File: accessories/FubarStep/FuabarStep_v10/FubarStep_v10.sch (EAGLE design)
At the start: 10 parts, among them IC1 7805, X1 DC21MMX

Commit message: More work.
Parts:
- removed AD: (no value), pinhead:PINHD-1X6
- removed IOL, POWER: (no value), pinhead:PINHD-1X8
- added C10, C11, C12, C13, C14, C15, C18, C19, C8, C9: .1uF, SparkFun-Capacitors:CAPPTH
- added C16, C17, C5: 100uF, SparkFun-Capacitors:CAP_POLPTH1
- added IC2, IC3: SN754410NE, texas:L293E
- added JP10, JP11, JP12, JP13, JP14, JP15, JP16, JP17, JP18, JP19, JP20, JP21, JP22, JP23, JP24, JP25, JP26, JP27, JP3, JP4, JP5, JP6: (no value), SparkFun-Connectors:M03LOCK
- added JP2: (no value), SparkFun-Connectors:M04SCREW_LOCK
- added JP7, JP8, JP9: (no value), SparkFun-Connectors:M04LOCK
- added LOGO1: OSHW-LOGOM, SparkFun-Aesthetics:OSHW-LOGOM
- C2: value 10uF -> 100uF; device SparkFun-Capacitors:CAP_POLPTH2 -> SparkFun-Capacitors:CAP_POLPTH1
- IC1: value 7805 -> OKI-78SR-5/1.5-W36H-C
- JP1: device pinhead:PINHD-1X10 -> SparkFun-Connectors:M04SCREW_LOCK
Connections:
- removed net AD0: AD.1
- removed net AD1: AD.2
- removed net AD2: AD.3
- removed net AD3: AD.4
- removed net AD4: AD.5
- removed net AD4/SDA: JP1.9
- removed net AD5: AD.6
- removed net AD5/SCL: JP1.10
- removed net AREF: JP1.8
- removed net IO0: IOL.1
- removed net IO1: IOL.2
- removed net IO2: IOL.3
- removed net IO3: IOL.4
- removed net IO4: IOL.5
- removed net IO5: IOL.6
- removed net IO6: IOL.7
- removed net IO7: IOL.8
- removed net IO8: JP1.1
- removed net IO9: JP1.2
- removed net MISO: JP1.5
- removed net MOSI: JP1.4
- removed net SCK: JP1.6
- removed net SS: JP1.3
- new net M1A1: IC2.1A
- new net M1A2: IC2.2A
- new net M1A3: IC2.3A
- new net M1A4: IC2.4A
- new net M1EN12: IC2.1-2EN, U$1.PIN7
- new net M1EN34: IC2.3-4EN, U$1.PIN8
- new net M1O1: C10.2, IC2.1Y, JP1.1
- new net M1O2: C11.2, IC2.2Y, JP1.2
- new net M1O3: C12.1, IC2.3Y, JP1.3
- new net M1O4: C9.1, IC2.4Y, JP1.4
- new net M2A1: IC3.1A
- new net M2A2: IC3.2A
- new net M2A3: IC3.3A
- new net M2A4: IC3.4A
- new net M2EN12: IC3.1-2EN, U$1.PIN9
- new net M2EN34: IC3.3-4EN, U$1.PIN10
- new net M2O1: C8.2, IC3.1Y, JP2.1
- new net M2O2: C13.2, IC3.2Y, JP2.2
- new net M2O3: C15.1, IC3.3Y, JP2.3
- new net M2O4: C14.1, IC3.4Y, JP2.4
- new net N$12: JP8.1
- new net N$2: JP18.1
- new net N$29: JP9.1
- new net N$3: JP19.1
- new net N$67: JP9.2
- new net N$68: JP9.3
- new net N$69: JP23.1
- new net N$87: JP22.1
- new net N$88: JP17.1
- new net N$89: JP16.1
- new net N$90: JP15.1
- new net N$91: JP14.1
- new net N$92: JP10.1
- new net N$93: JP11.1
- new net N$94: JP12.1
- new net N$95: JP13.1
- new net N$96: JP24.1
- new net N$97: JP25.1
- new net RX: JP7.3, U$1.PIN28
- new net SERVO1: JP6.1
- new net SERVO2: JP3.1
- new net SERVO3: JP4.1
- new net SERVO4: JP5.1
- new net TX: JP7.2, U$1.PIN29
- net +3V3: no longer POWER.4
- net +5V: now also C18.1, C19.1, C5.+, IC2.VCC1, IC3.VCC1, JP10.2, JP11.2, JP12.2, JP13.2, JP14.2, JP15.2, JP16.2, JP17.2, JP18.2, JP19.2, JP20.2, JP21.2, JP22.2, JP23.2, JP24.2, JP25.2, JP26.2, JP27.2, JP3.2, JP4.2, JP5.2, JP6.2, JP7.1, U$1.VIN, U$2.VIN; no longer POWER.2, POWER.5, U$1.5V_OUT, U$2.5V_OUT
- net GND: now also C10.1, C11.1, C12.2, C13.1, C14.2, C15.2, C16.-, C17.-, C18.2, C19.2, C5.-, C8.1, C9.2, IC2.GND1, IC2.GND2, IC2.GND3, IC2.GND4, IC3.GND1, IC3.GND2, IC3.GND3, IC3.GND4, JP10.3, JP11.3, JP12.3, JP13.3, JP14.3, JP15.3, JP16.3, JP17.3, JP18.3, JP19.3, JP20.3, JP21.3, JP22.3, JP23.3, JP24.3, JP25.3, JP26.3, JP27.3, JP3.3, JP4.3, JP5.3, JP6.3, JP7.4, JP8.4, JP9.4; no longer JP1.7, POWER.6, POWER.7
- net N$11: now also JP20.1; no longer U$1.PIN7
- net N$13: now also JP8.2; no longer U$1.PIN8
- net N$14: now also JP8.3; no longer U$1.PIN9
- net N$15: now also JP21.1; no longer U$1.PIN10
- net N$33: now also JP26.1; no longer U$1.PIN29
- net N$34: now also JP27.1; no longer U$1.PIN28
- net RESET: no longer POWER.3
- net VIN: now also C16.+, C17.+, IC2.VCC2, IC3.VCC2; no longer POWER.8, U$1.VIN, U$2.VIN
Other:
- note added: "Fubarino Stepper Shield"
- note removed: "0"
- note removed: "1"
- note removed: "10"
- note removed: "11"
- note removed: "12"
- note removed: "13"
- note removed: "2"
- note removed: "3"
- note removed: "4"
- note removed: "5"
- note removed: "6"
- note removed: "7"
- note removed: "8"
- note removed: "9"
- note removed: "Fubarino Arduino Uno Adapter Board"
- note removed: "SCL"
- note removed: "SDA"
- moved on the sheet: C1, C2, IC1, U$1, U$2

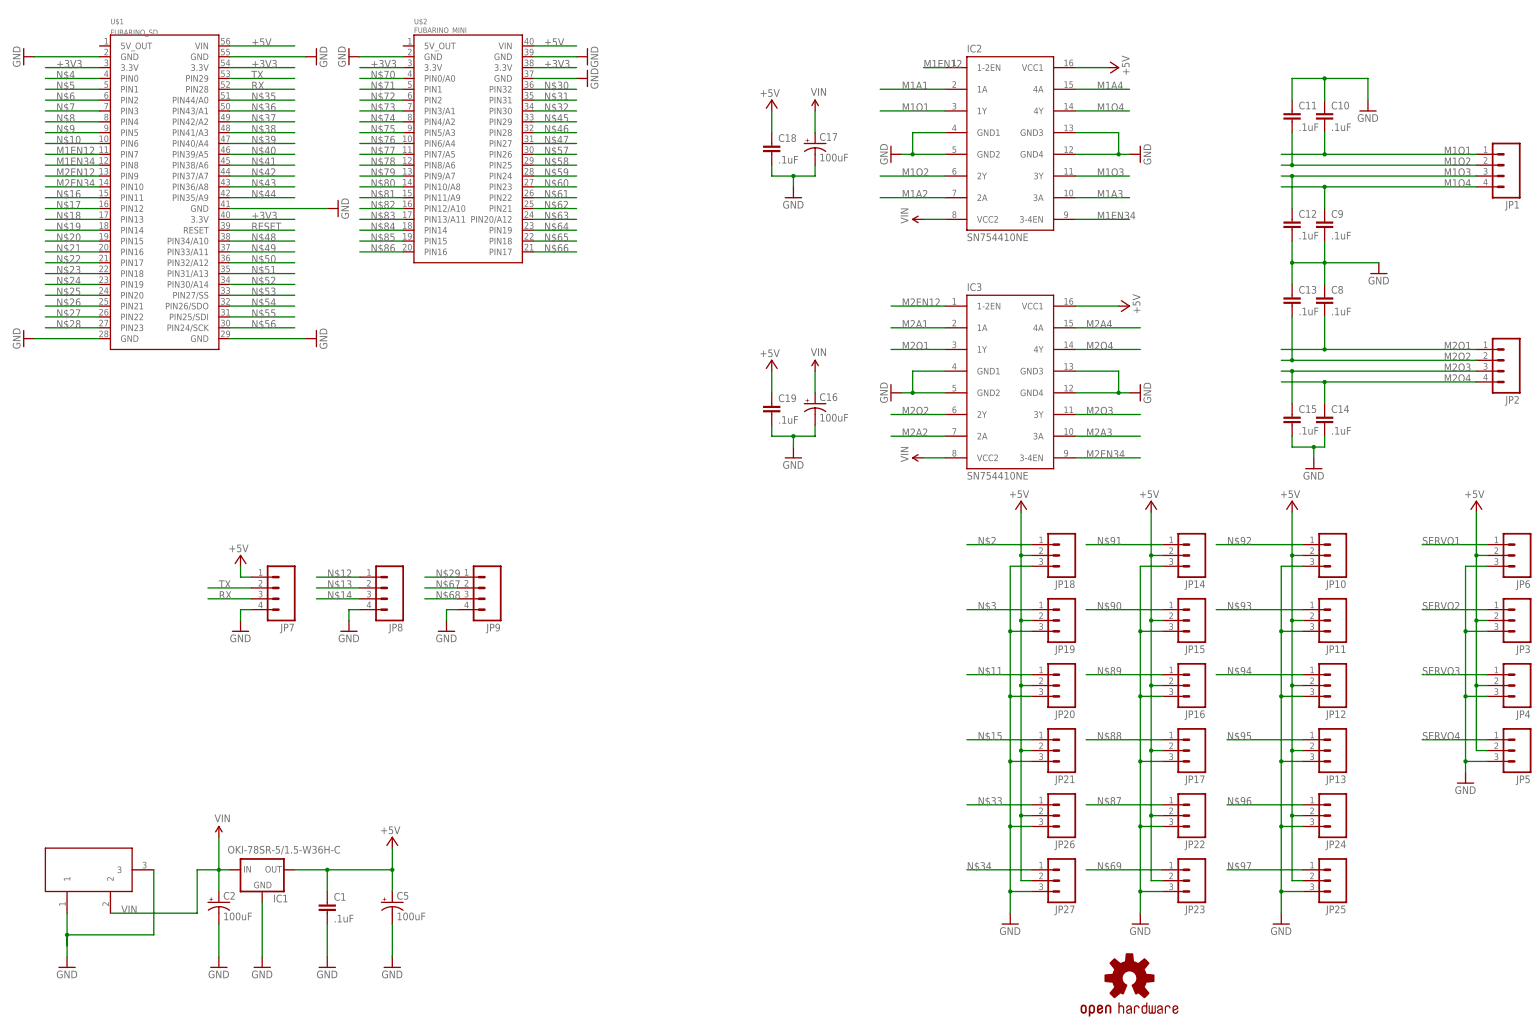
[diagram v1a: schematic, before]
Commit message: Renamed board from thin to normal, added all Mini routing except for 2 pins (maybe TX/RX?) Almost done!
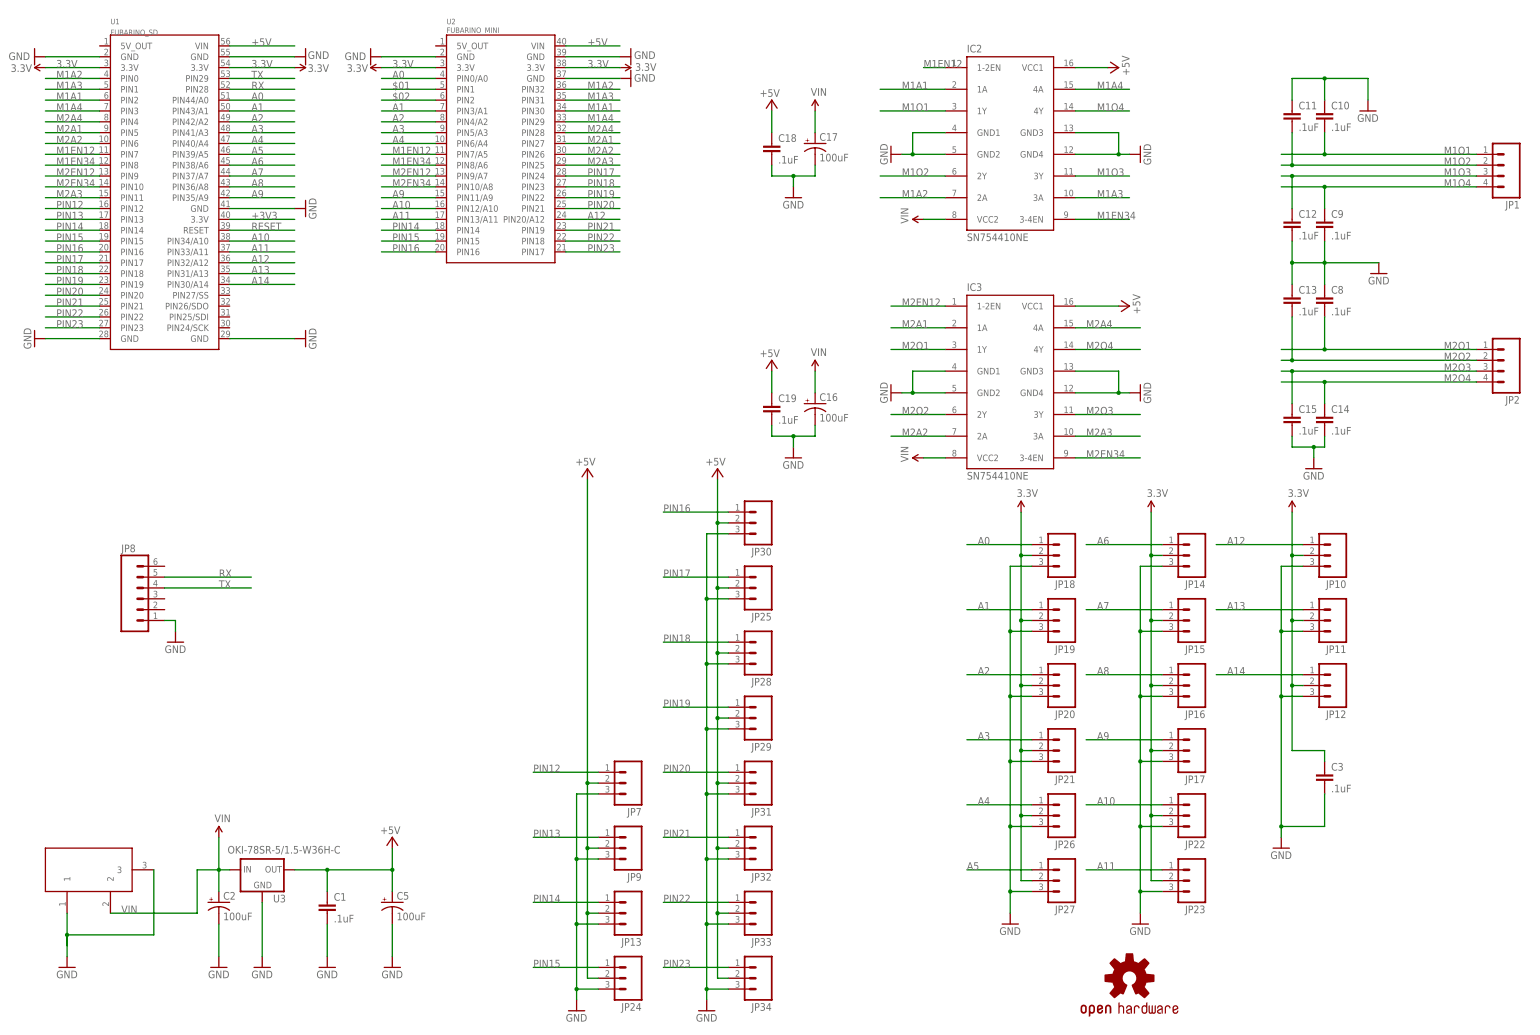
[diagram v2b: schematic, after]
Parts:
- removed IC1: OKI-78SR-5/1.5-W36H-C, SparkFun-PowerIC:V_REG_78XXSIDE
- removed JP3, JP4, JP5, JP6: (no value), SparkFun-Connectors:M03LOCK
- removed U$2: FUBARINO_MINI, SchmalzHausPublic:FUBARINO_MINI
- added C3: .1uF, SparkFun-Capacitors:CAPPTH
- added JP28, JP29, JP30, JP31, JP32, JP33, JP34: (no value), SparkFun-Connectors:M03PTH
- added U2: FUBARINO_MINI, SchmalzHausPublic:FUBARINO_MINI
- added U3: OKI-78SR-5/1.5-W36H-C, SparkFun-PowerIC:V_REG_78XXSINK
- JP10, JP11, JP12, JP13, JP14, JP15, JP16, JP17, JP18, JP19, JP20, JP21, JP22, JP23, JP24, JP25, JP26, JP27: device SparkFun-Connectors:M03LOCK -> SparkFun-Connectors:M03PTH
- JP7, JP9: device SparkFun-Connectors:M04LOCK -> SparkFun-Connectors:M03PTH
- JP8: device SparkFun-Connectors:M04LOCK -> SparkFun-Connectors:M06LOCK
- renumbered U$1 to U1
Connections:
- removed net N$10: U1.PIN6
- removed net N$11: JP20.1
- removed net N$12: JP8.1
- removed net N$13: JP8.2
- removed net N$14: JP8.3
- removed net N$15: JP21.1
- removed net N$16: U1.PIN11
- removed net N$17: U1.PIN12
- removed net N$18: U1.PIN13
- removed net N$19: U1.PIN14
- removed net N$2: JP18.1
- removed net N$20: U1.PIN15
- removed net N$21: U1.PIN16
- removed net N$22: U1.PIN17
- removed net N$23: U1.PIN18
- removed net N$24: U1.PIN19
- removed net N$25: U1.PIN20
- removed net N$26: U1.PIN21
- removed net N$27: U1.PIN22
- removed net N$28: U1.PIN23
- removed net N$29: JP9.1
- removed net N$3: JP19.1
- removed net N$30: U$2.PIN32
- removed net N$31: U$2.PIN31
- removed net N$32: U$2.PIN30
- removed net N$33: JP26.1
- removed net N$34: JP27.1
- removed net N$35: U1.PIN44/A0
- removed net N$36: U1.PIN43/A1
- removed net N$37: U1.PIN42/A2
- removed net N$38: U1.PIN41/A3
- removed net N$39: U1.PIN40/A4
- removed net N$4: U1.PIN0
- removed net N$40: U1.PIN39/A5
- removed net N$41: U1.PIN38/A6
- removed net N$42: U1.PIN37/A7
- removed net N$43: U1.PIN36/A8
- removed net N$44: U1.PIN35/A9
- removed net N$45: U$2.PIN29
- removed net N$46: U$2.PIN28
- removed net N$47: U$2.PIN27
- removed net N$48: U1.PIN34/A10
- removed net N$49: U1.PIN33/A11
- removed net N$5: U1.PIN1
- removed net N$50: U1.PIN32/A12
- removed net N$51: U1.PIN31/A13
- removed net N$52: U1.PIN30/A14
- removed net N$53: U1.PIN27/SS
- removed net N$54: U1.PIN26/SDO
- removed net N$55: U1.PIN25/SDI
- removed net N$56: U1.PIN24/SCK
- removed net N$57: U$2.PIN26
- removed net N$58: U$2.PIN25
- removed net N$59: U$2.PIN24
- removed net N$6: U1.PIN2
- removed net N$60: U$2.PIN23
- removed net N$61: U$2.PIN22
- removed net N$62: U$2.PIN21
- removed net N$63: U$2.PIN20/A12
- removed net N$64: U$2.PIN19
- removed net N$65: U$2.PIN18
- removed net N$66: U$2.PIN17
- removed net N$67: JP9.2
- removed net N$68: JP9.3
- removed net N$69: JP23.1
- removed net N$7: U1.PIN3
- removed net N$70: U$2.PIN0/A0
- removed net N$71: U$2.PIN1
- removed net N$72: U$2.PIN2
- removed net N$73: U$2.PIN3/A1
- removed net N$74: U$2.PIN4/A2
- removed net N$75: U$2.PIN5/A3
- removed net N$76: U$2.PIN6/A4
- removed net N$77: U$2.PIN7/A5
- removed net N$78: U$2.PIN8/A6
- removed net N$79: U$2.PIN9/A7
- removed net N$8: U1.PIN4
- removed net N$80: U$2.PIN10/A8
- removed net N$81: U$2.PIN11/A9
- removed net N$82: U$2.PIN12/A10
- removed net N$83: U$2.PIN13/A11
- removed net N$84: U$2.PIN14
- removed net N$85: U$2.PIN15
- removed net N$86: U$2.PIN16
- removed net N$87: JP22.1
- removed net N$88: JP17.1
- removed net N$89: JP16.1
- removed net N$9: U1.PIN5
- removed net N$90: JP15.1
- removed net N$91: JP14.1
- removed net N$92: JP10.1
- removed net N$93: JP11.1
- removed net N$94: JP12.1
- removed net N$95: JP13.1
- removed net N$96: JP24.1
- removed net N$97: JP25.1
- removed net SERVO1: JP6.1
- removed net SERVO2: JP3.1
- removed net SERVO3: JP4.1
- removed net SERVO4: JP5.1
- new net $01: U2.PIN1
- new net $02: U2.PIN2
- new net 3.3V: C3.1, JP10.2, JP11.2, JP12.2, JP14.2, JP15.2, JP16.2, JP17.2, JP18.2, JP19.2, JP20.2, JP21.2, JP22.2, JP23.2, JP26.2, JP27.2, U1.3.3V@1, U1.3.3V@3, U2.3.3V@1, U2.3.3V@3
- new net A0: JP18.1, U1.PIN44/A0, U2.PIN0/A0
- new net A1: JP19.1, U1.PIN43/A1, U2.PIN3/A1
- new net A10: JP22.1, U1.PIN34/A10, U2.PIN12/A10
- new net A11: JP23.1, U1.PIN33/A11, U2.PIN13/A11
- new net A12: JP10.1, U1.PIN32/A12, U2.PIN20/A12
- new net A13: JP11.1, U1.PIN31/A13
- new net A14: JP12.1, U1.PIN30/A14
- new net A2: JP20.1, U1.PIN42/A2, U2.PIN4/A2
- new net A3: JP21.1, U1.PIN41/A3, U2.PIN5/A3
- new net A4: JP26.1, U1.PIN40/A4, U2.PIN6/A4
- new net A5: JP27.1, U1.PIN39/A5
- new net A6: JP14.1, U1.PIN38/A6
- new net A7: JP15.1, U1.PIN37/A7
- new net A8: JP16.1, U1.PIN36/A8
- new net A9: JP17.1, U1.PIN35/A9, U2.PIN11/A9
- new net PIN12: JP7.1, U1.PIN12
- new net PIN13: JP9.1, U1.PIN13
- new net PIN14: JP13.1, U1.PIN14, U2.PIN14
- new net PIN15: JP24.1, U1.PIN15, U2.PIN15
- new net PIN16: JP30.1, U1.PIN16, U2.PIN16
- new net PIN17: JP25.1, U1.PIN17, U2.PIN24
- new net PIN18: JP28.1, U1.PIN18, U2.PIN23
- new net PIN19: JP29.1, U1.PIN19, U2.PIN22
- new net PIN20: JP31.1, U1.PIN20, U2.PIN21
- new net PIN21: JP32.1, U1.PIN21, U2.PIN19
- new net PIN22: JP33.1, U1.PIN22, U2.PIN18
- new net PIN23: JP34.1, U1.PIN23, U2.PIN17
- net +3V3: no longer U$2.3.3V@1, U$2.3.3V@3, U1.3.3V@1, U1.3.3V@3
- net +5V: now also JP28.2, JP29.2, JP30.2, JP31.2, JP32.2, JP33.2, JP34.2, JP7.2, JP9.2, U2.VIN, U3.OUT; no longer IC1.OUT, JP10.2, JP11.2, JP12.2, JP14.2, JP15.2, JP16.2, JP17.2, JP18.2, JP19.2, JP20.2, JP21.2, JP22.2, JP23.2, JP26.2, JP27.2, JP3.2, JP4.2, JP5.2, JP6.2, JP7.1, U$2.VIN
- net GND: now also C3.2, JP28.3, JP29.3, JP30.3, JP31.3, JP32.3, JP33.3, JP34.3, JP7.3, JP8.1, JP9.3, U2.GND@1, U2.GND@4, U2.GND@5, U3.GND; no longer IC1.GND, JP3.3, JP4.3, JP5.3, JP6.3, JP7.4, JP8.4, JP9.4, U$2.GND@1, U$2.GND@4, U$2.GND@5
- net M1A1: now also U1.PIN2, U2.PIN30
- net M1A2: now also U1.PIN0, U2.PIN32
- net M1A3: now also U1.PIN1, U2.PIN31
- net M1A4: now also U1.PIN3, U2.PIN29
- net M1EN12: now also U2.PIN7/A5
- net M1EN34: now also U2.PIN8/A6
- net M2A1: now also U1.PIN5, U2.PIN27
- net M2A2: now also U1.PIN6, U2.PIN26
- net M2A3: now also U1.PIN11, U2.PIN25
- net M2A4: now also U1.PIN4, U2.PIN28
- net M2EN12: now also U2.PIN9/A7
- net M2EN34: now also U2.PIN10/A8
- net RX: now also JP8.5; no longer JP7.3
- net TX: now also JP8.4; no longer JP7.2
- net VIN: now also U3.IN; no longer IC1.IN
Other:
- moved on the sheet: JP13, JP24, JP25

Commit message: Version 1.0 done - routed, schematic done (with license), just need to add BOM now.
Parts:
- added U$1: SCHMALZHAUSSCHMALZHAUS_SMALL, SchmalzHaus:SCHMALZHAUSSCHMALZHAUS_SMALL
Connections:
- removed net $01: U2.PIN1
- removed net $02: U2.PIN2
- net PIN12: now also U2.PIN1
- net PIN13: now also U2.PIN2
- net PIN22: no longer U2.PIN18
- net PIN23: no longer U2.PIN17
- net RX: now also JP8.4, U2.PIN17; no longer JP8.5
- net TX: now also JP8.5, U2.PIN18; no longer JP8.4
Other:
- note added: "12V DC in (anywhere from 7V to 24V OK)"
- note added: "Analog Input/3.3v only GPIO"
- note added: "Copyright 2013 Brian Schmalz and Rick Anderson Copyright and related rights are licensed under the Solderpad Hardware License, Version 0.51 (the “License”);"
- note added: "FTDI Serial"
- note added: "Motor 1"
- note added: "Motor 2"
- note added: "Power Supply"
- note added: "RC Servo/5V tollerant GPIO"
- note added: "See the License for the specific language governing permissions and limitations under the License."
- note added: "chipKIT Fubarino (use only one a time)"
- note added: "software, hardware and materials distributed under this License is distributed on an “AS IS” BASIS, WITHOUT WARRANTIES OR CONDITIONS OF ANY KIND, either express or implied."
- note added: "you may not use this file except in compliance with the License. You may obtain a copy of the License at http://solderpad.org/licenses/SHL-0.51. Unless required by applicable law or agreed to in writing,"
- moved on the sheet: C1, C10, C11, C12, C13, C14, C15, C16, C17, C18, C19, C2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
